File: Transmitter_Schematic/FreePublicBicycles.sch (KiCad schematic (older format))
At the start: 41 parts, among them J1 Conn_01x04_Female, Q1 PN2222A, Q2 IRF4905, SW1 Button, U1 ATmega328-PU, U2 MP1584, U3 BA33BC0T, U4 S9V11F5, U5 RFM95W-868S2, U6 NEO-6M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

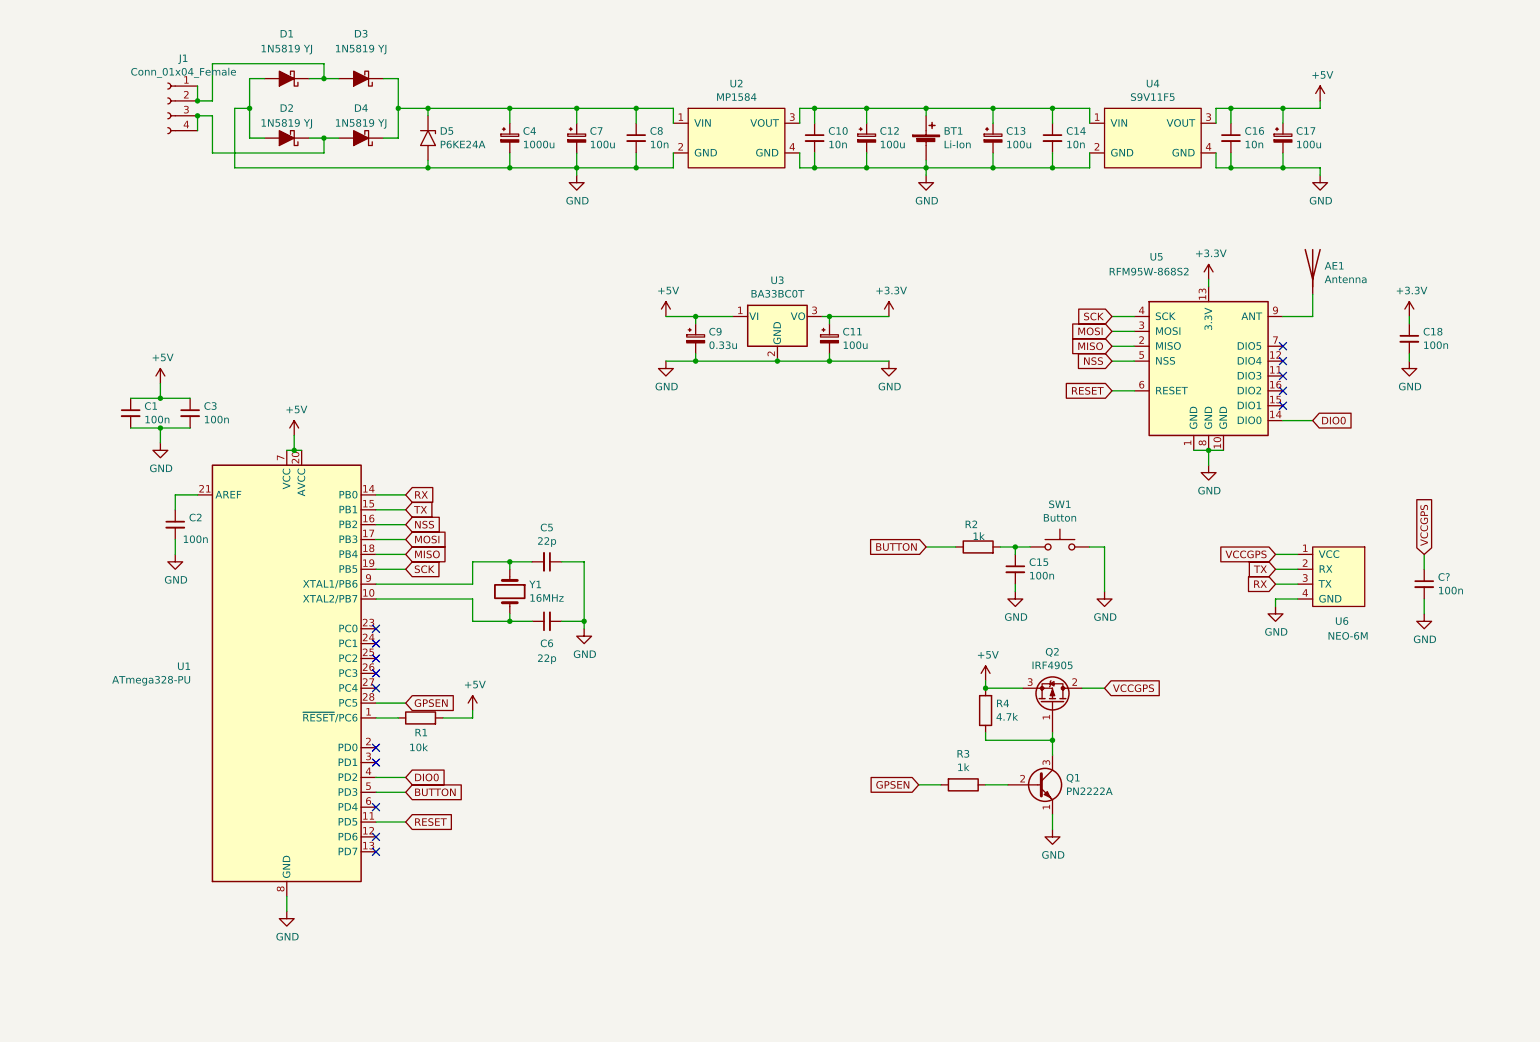
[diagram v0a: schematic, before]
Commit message: Fixed Transmitter PCB Spacing
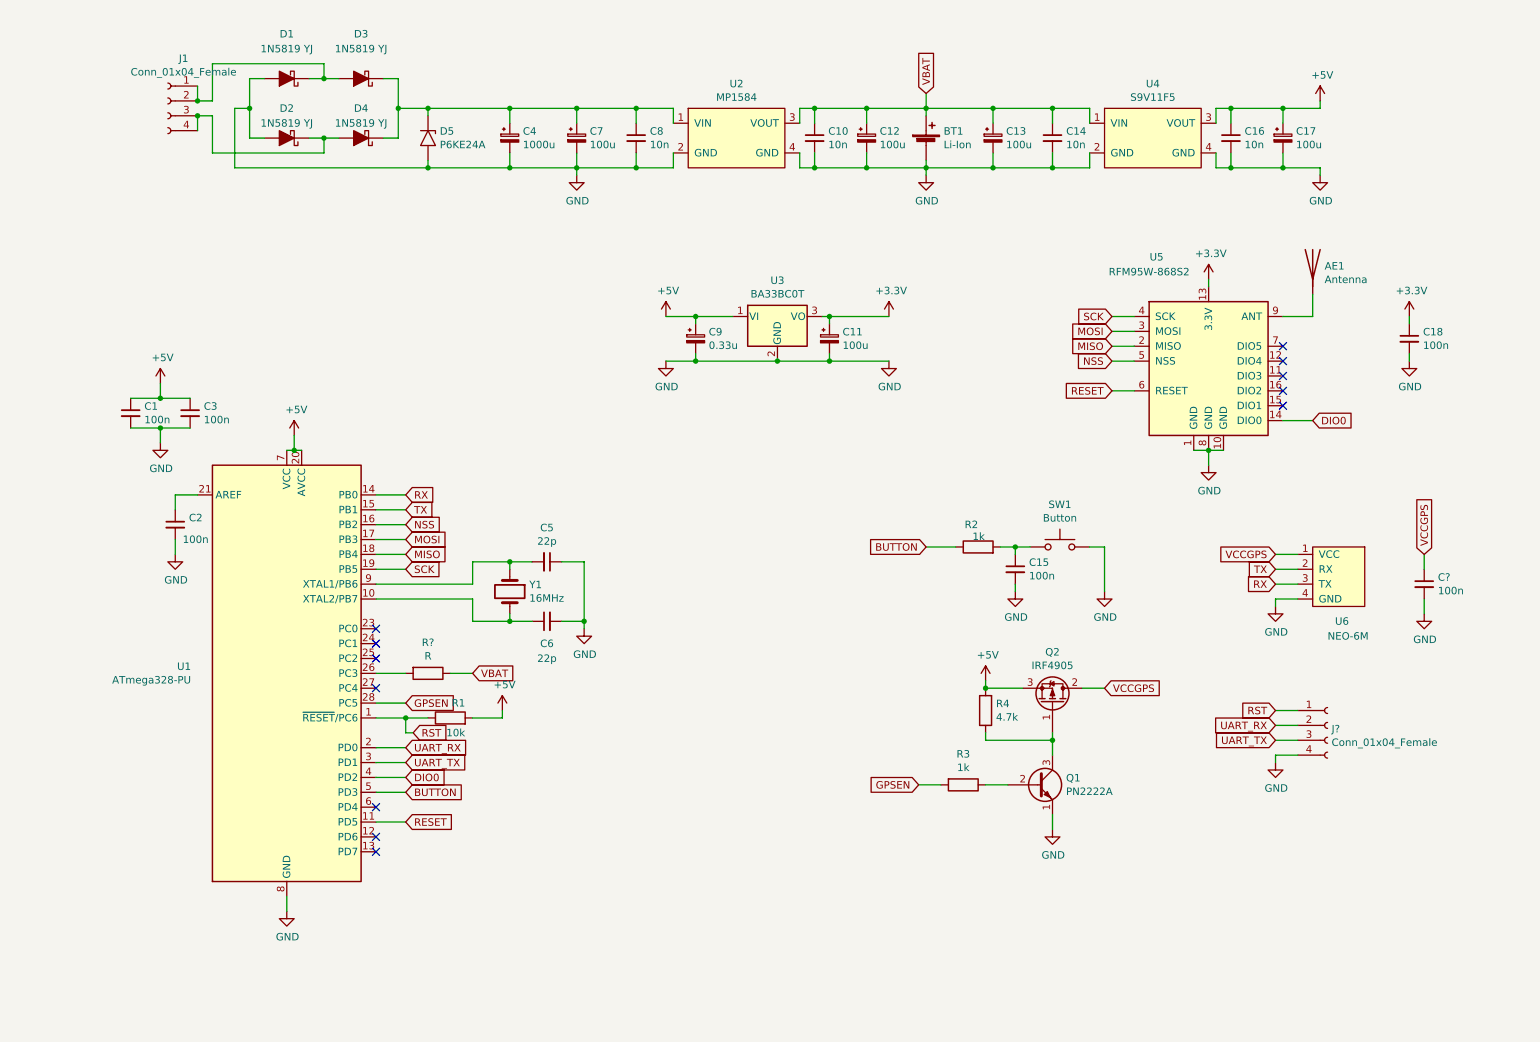
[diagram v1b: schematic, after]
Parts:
- added J?: Conn_01x04_Female, symbol Connector:Conn_01x04_Female
- added R?: R, symbol Device:R
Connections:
- net GND: now also J?.4 (Pin_4)
- net RST: now reaches R1.1, U1.1 (~RESET~/PC6)
- net RST: now also J?.1 (Pin_1)
- net UART_RX: now reaches U1.2 (PD0)
- net UART_RX: now also J?.2 (Pin_2)
- net at U1.26 (PC3): now also R?.2
- net UART_TX: now reaches U1.3 (PD1)
- net UART_TX: now also J?.3 (Pin_3)
- net VBAT: now reaches BT1.1 (+), C10.1, C12.1, C13.1, C14.1, U2.3 (VOUT), U4.1 (VIN)
- net VBAT: now also R?.1
- no-connect marks 15 -> 12
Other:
- moved on the sheet: R1
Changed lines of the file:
@@
 	1    0    0    -1
 $EndComp
-Wire Wire Line
-	3150 5350 3300 5350
 $Comp
 L Device:R R1
 U 1 1 5E3312B4
-P 3450 5350
-F 0 "R1" V 3350 5300 50  0000 L CNN
-F 1 "10k" V 3250 5300 50  0000 L CNN
-F 2 "" V 3380 5350 50  0001 C CNN
-F 3 "~" H 3450 5350 50  0001 C CNN
-	1    3450 5350
+P 3650 5350
+F 0 "R1" V 3750 5250 50  0000 L CNN
+F 1 "10k" V 3550 5250 50  0000 L CNN
+F 2 "" V 3580 5350 50  0001 C CNN
+F 3 "~" H 3650 5350 50  0001 C CNN
+	1    3650 5350
 	0    -1   -1   0
 $EndComp
@@
 L power:+5V #PWR06
 U 1 1 5E336D89
-P 3800 5300
-F 0 "#PWR06" H 3800 5150 50  0001 C CNN
-F 1 "+5V" H 3815 5473 50  0000 C CNN
-F 2 "" H 3800 5300 50  0001 C CNN
-F 3 "" H 3800 5300 50  0001 C CNN
-	1    3800 5300
+P 4000 5300
+F 0 "#PWR06" H 4000 5150 50  0001 C CNN
+F 1 "+5V" H 4015 5473 50  0000 C CNN
+F 2 "" H 4000 5300 50  0001 C CNN
+F 3 "" H 4000 5300 50  0001 C CNN
+	1    4000 5300
 	1    0    0    -1
 $EndComp
@@
 BUTTON
 Wire Wire Line
-	3600 5350 3800 5350
-Wire Wire Line
-	3800 5350 3800 5300
+	3800 5350 4000 5350
+Wire Wire Line
+	4000 5350 4000 5300
 $Comp
 L power:+5V #PWR09
@@
 NoConn ~ 3150 4850
 NoConn ~ 3150 4950
-NoConn ~ 3150 5050
 NoConn ~ 3150 5150
-NoConn ~ 3150 5550
-NoConn ~ 3150 5650
 NoConn ~ 3150 5950
 NoConn ~ 3150 6150
@@
 NoConn ~ 3150 4750
 NoConn ~ 9250 3250
+Wire Wire Line
+	3150 5050 3350 5050
+$Comp
+L Device:R R?
+U 1 1 5E3C2A29
+P 3500 5050
+F 0 "R?" V 3293 5050 50  0000 C CNN
+F 1 "R" V 3384 5050 50  0000 C CNN
+F 2 "" V 3430 5050 50  0001 C CNN
+F 3 "~" H 3500 5050 50  0001 C CNN
+	1    3500 5050
+	0    1    1    0
+$EndComp
+Wire Wire Line
+	3650 5050 3800 5050
+Text GLabel 3800 5050 2    50   Input ~ 0
+VBAT
+Wire Wire Line
+	6850 1250 6850 1150
+Text GLabel 6850 1150 1    50   Input ~ 0
+VBAT
+Wire Wire Line
+	3350 5450 3400 5450
+Text GLabel 3400 5450 2    50   Input ~ 0
+RST
+Wire Wire Line
+	3350 5450 3350 5350
+Wire Wire Line
+	3150 5350 3350 5350
+Wire Wire Line
+	3350 5350 3500 5350
+Connection ~ 3350 5350
+Wire Wire Line
+	3150 5550 3350 5550
+Wire Wire Line
+	3150 5650 3350 5650
+Text GLabel 3350 5550 2    50   Input ~ 0
+UART_RX
+Text GLabel 3350 5650 2    50   Input ~ 0
+UART_TX
+$Comp
+L Connector:Conn_01x04_Female J?
+U 1 1 5E436444
+P 9550 5400
+F 0 "J?" H 9577 5376 50  0000 L CNN
+F 1 "Conn_01x04_Female" H 9577 5285 50  0000 L CNN
+F 2 "" H 9550 5400 50  0001 C CNN
+F 3 "~" H 9550 5400 50  0001 C CNN
+	1    9550 5400
+	1    0    0    -1
+$EndComp
+Wire Wire Line
+	9350 5300 9200 5300
+Wire Wire Line
+	9350 5400 9200 5400
+Wire Wire Line
+	9350 5500 9200 5500
+Wire Wire Line
+	9350 5600 9200 5600
+Wire Wire Line
+	9200 5600 9200 5650
+$Comp
+L power:GND #PWR?
+U 1 1 5E464716
+P 9200 5650
+F 0 "#PWR?" H 9200 5400 50  0001 C CNN
+F 1 "GND" H 9205 5477 50  0000 C CNN
+F 2 "" H 9200 5650 50  0001 C CNN
+F 3 "" H 9200 5650 50  0001 C CNN
+	1    9200 5650
+	1    0    0    -1
+$EndComp
+Text GLabel 9200 5500 0    50   Input ~ 0
+UART_TX
+Text GLabel 9200 5400 0    50   Input ~ 0
+UART_RX
+Text GLabel 9200 5300 0    50   Input ~ 0
+RST
 $EndSCHEMATC

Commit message: Added changes to schematics
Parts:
- R5: renamed from R?; value R -> 10К
- gave numbers to parts that had none: 2
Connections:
- net GND: no longer C5.1, C6.2
- new net: C5.1, C6.2
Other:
- note added: "Communication Unit"
- note added: "Control Unit"
- note added: "GPS Unit"
- note added: "Power Supply Unit"
- moved on the sheet: AE1, BT1, C1, C10, C11, C12, C13, C14, C15, C16, C17, C18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

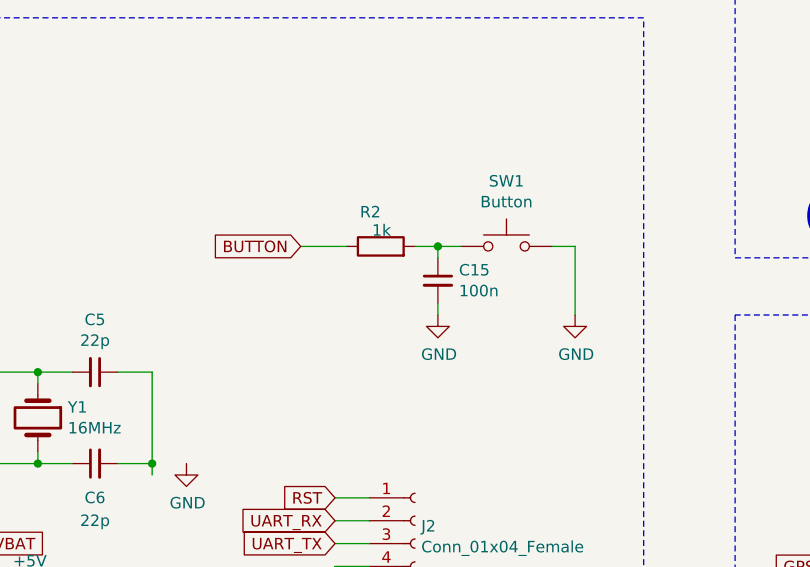
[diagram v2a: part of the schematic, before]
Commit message: Changed message identification
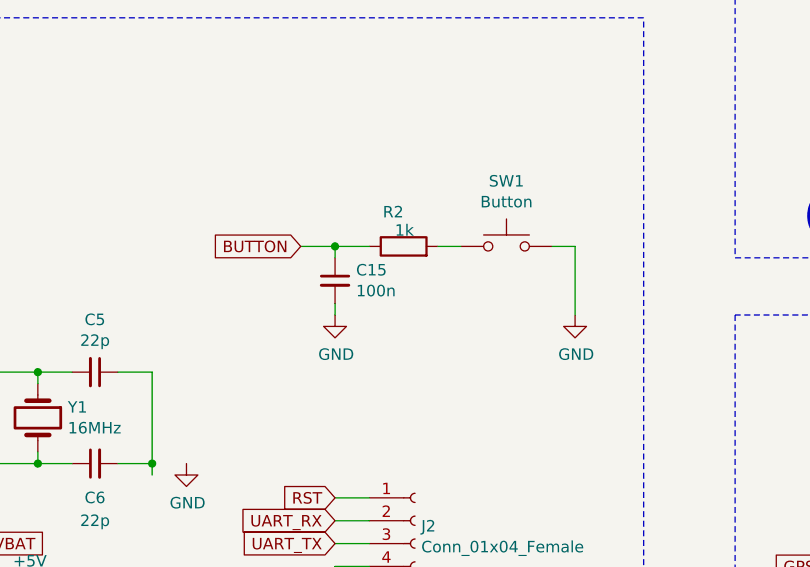
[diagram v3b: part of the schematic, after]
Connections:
- net BUTTON: now also C15.1
- net at R2.2, SW1.1: no longer C15.1
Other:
- moved on the sheet: C15, R2
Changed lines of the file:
@@
 L Device:C_Small C15
 U 1 1 5E2EF3C9
-P 5250 4400
-F 0 "C15" H 5342 4446 50  0000 L CNN
-F 1 "100n" H 5342 4355 50  0000 L CNN
-F 2 "" H 5250 4400 50  0001 C CNN
-F 3 "~" H 5250 4400 50  0001 C CNN
-	1    5250 4400
-	1    0    0    -1
-$EndComp
-Wire Wire Line
-	5250 4500 5250 4550
-Wire Wire Line
-	5250 4250 5250 4300
-Wire Wire Line
-	5350 4250 5250 4250
+P 4800 4400
+F 0 "C15" H 4892 4446 50  0000 L CNN
+F 1 "100n" H 4892 4355 50  0000 L CNN
+F 2 "" H 4800 4400 50  0001 C CNN
+F 3 "~" H 4800 4400 50  0001 C CNN
+	1    4800 4400
+	1    0    0    -1
+$EndComp
+Wire Wire Line
+	4800 4500 4800 4550
+Wire Wire Line
+	4800 4250 4800 4300
 $Comp
 L Device:R R2
 U 1 1 5E3039C3
-P 5000 4250
-F 0 "R2" V 5150 4250 50  0000 L CNN
-F 1 "1k" V 5070 4205 50  0000 L CNN
-F 2 "" V 4930 4250 50  0001 C CNN
-F 3 "~" H 5000 4250 50  0001 C CNN
-	1    5000 4250
+P 5100 4250
+F 0 "R2" V 5250 4250 50  0000 L CNN
+F 1 "1k" V 5170 4205 50  0000 L CNN
+F 2 "" V 5030 4250 50  0001 C CNN
+F 3 "~" H 5100 4250 50  0001 C CNN
+	1    5100 4250
 	0    -1   -1   0
 $EndComp
 Wire Wire Line
-	5250 4250 5150 4250
-Connection ~ 5250 4250
-Wire Wire Line
-	4650 4250 4850 4250
+	4650 4250 4800 4250
 $Comp
 L power:GND #PWR014
 U 1 1 5E341971
-P 5250 4550
-F 0 "#PWR014" H 5250 4300 50  0001 C CNN
-F 1 "GND" H 5255 4377 50  0000 C CNN
-F 2 "" H 5250 4550 50  0001 C CNN
-F 3 "" H 5250 4550 50  0001 C CNN
-	1    5250 4550
+P 4800 4550
+F 0 "#PWR014" H 4800 4300 50  0001 C CNN
+F 1 "GND" H 4805 4377 50  0000 C CNN
+F 2 "" H 4800 4550 50  0001 C CNN
+F 3 "" H 4800 4550 50  0001 C CNN
+	1    4800 4550
 	1    0    0    -1
 $EndComp
@@
 Text Notes 3150 2550 0    200  ~ 0
 Power Supply Unit
+Connection ~ 4800 4250
+Wire Wire Line
+	4800 4250 4950 4250
+Wire Wire Line
+	5250 4250 5350 4250
 $EndSCHEMATC
